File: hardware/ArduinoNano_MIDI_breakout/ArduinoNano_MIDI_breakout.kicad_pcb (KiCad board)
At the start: 2 copper layers, 68.7 x 101.3 mm, 39 parts, among them J2 MIDI OUT, J3 MIDI IN, J4 I2C, J5 Conn_01x15_Male, J6 Conn_01x15_Male, J7 Barrel_Jack_Switch, Q1 2N3904, SW1 RotaryEncoder_Switch, SW2 SW_Push, SW3 SW_Push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

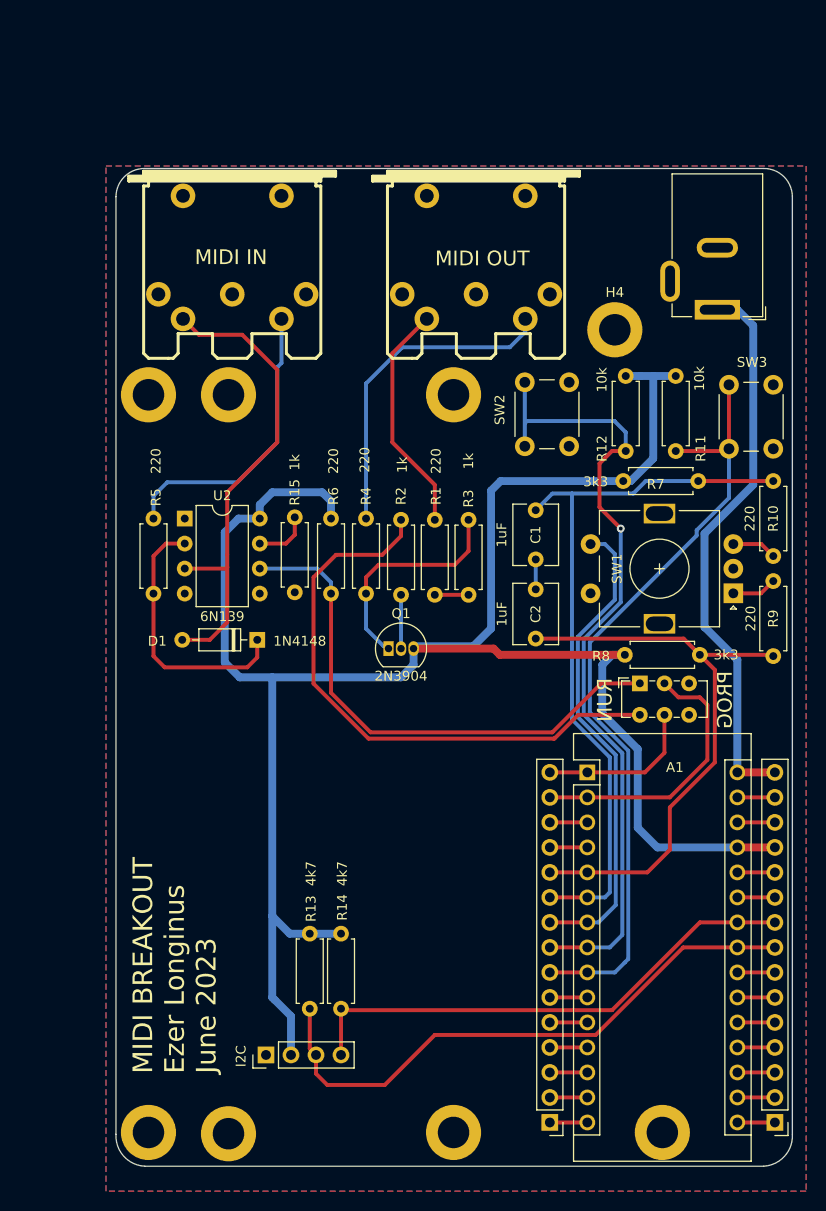
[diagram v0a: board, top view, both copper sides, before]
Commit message: Fixed MIDI pinout swap
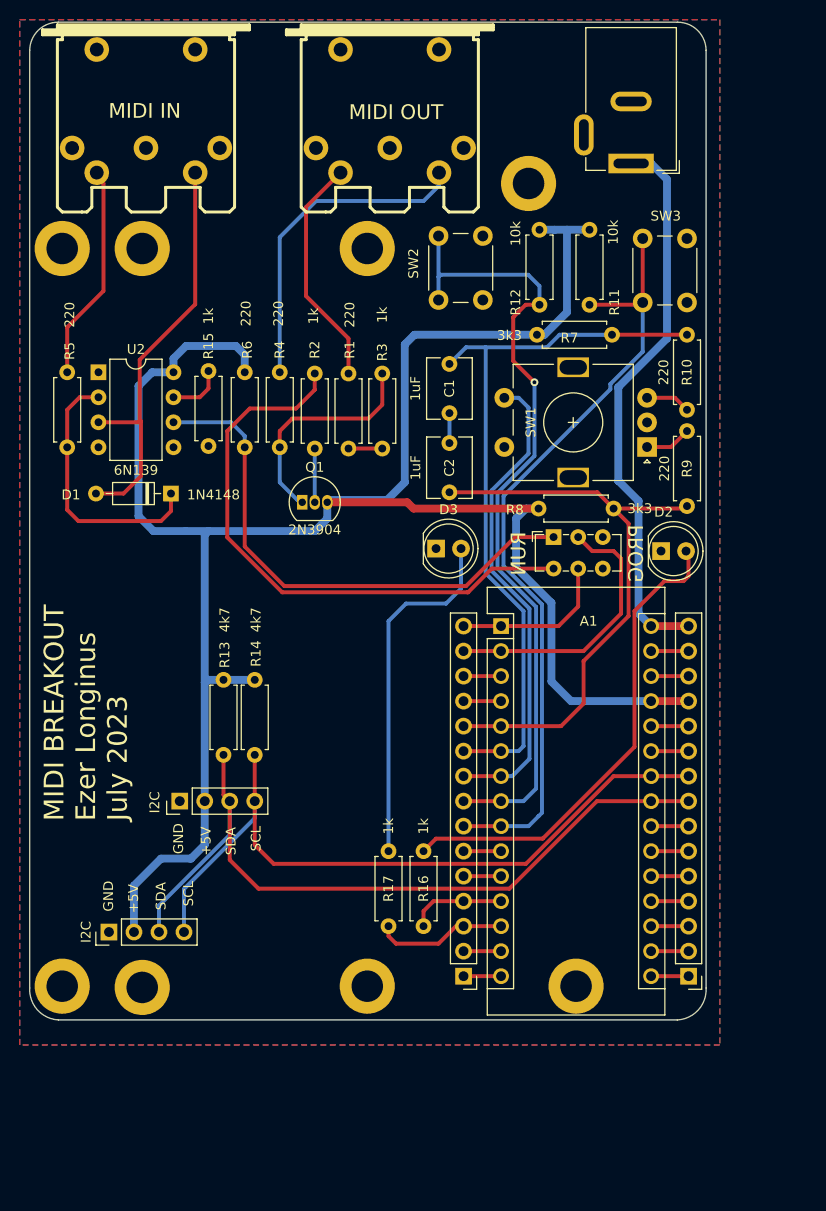
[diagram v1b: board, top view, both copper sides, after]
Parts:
- added D2: LED, LED_THT:LED_D5.0mm, F.Cu at (168.8, 94.4)
- added D3: LED, LED_THT:LED_D5.0mm, F.Cu at (145.9, 94.1)
- added I2C: I2C, Connector_PinHeader_2.54mm:PinHeader_1x04_P2.54mm_Vertical, F.Cu at (112.7, 133.1)
- added R16: 1k, Resistor_THT:R_Axial_DIN0207_L6.3mm_D2.5mm_P7.62mm_Horizontal, F.Cu at (144.7, 132.5)
- added R17: 1k, Resistor_THT:R_Axial_DIN0207_L6.3mm_D2.5mm_P7.62mm_Horizontal, F.Cu at (141.1, 132.5)
- moved J4 27.2 mm to (119.9, 119.8)
- moved R13 27.2 mm to (124.3, 115.1)
- moved R14 27.2 mm to (127.5, 115.1)
- moved R9 17.6 mm to (171.4, 89.8)
- moved A1 17.3 mm to (152.5, 102.0)
- moved C2 17.3 mm to (147.3, 88.4)
- moved H1 17.3 mm to (160.1, 138.6)
- moved H6 17.3 mm to (138.9, 138.6)
- moved J2 17.3 mm to (141.2, 50.4)
- moved J5 17.3 mm to (171.6, 137.5)
- moved R1 17.3 mm to (137.0, 76.3)
- moved R15 17.3 mm to (122.8, 76.1)
- moved R3 17.3 mm to (140.5, 76.3)
- moved R4 17.3 mm to (130.0, 83.8)
- moved SW4 17.3 mm to (157.9, 92.9)
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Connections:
- J3 pad 4: Net-(D1-Pad2) -> Net-(J3-Pad4)
- J3 pad 5: Net-(J3-Pad5) -> Net-(D1-Pad2)
- R5 pad 1: Net-(J3-Pad5) -> Net-(J3-Pad4)
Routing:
- net Net-(D2-Pad2): track 0.00 -> 49.1 mm
- net Net-(D3-Pad2): track 0.00 -> 36.2 mm
- net Net-(J3-Pad5): track 30.1 -> 0.00 mm
- net Net-(J3-Pad4): track 0.00 -> 22.1 mm
- net SCL1: track 52.5 -> 74.0 mm
- net SDA1: track 60.4 -> 79.4 mm
- net D10: track 3.81 -> 13.5 mm
- net D9: track 3.81 -> 9.82 mm
- net Net-(D1-Pad2): track 49.1 -> 43.3 mm
- net +5V: track 208.9 -> 212.8 mm
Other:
- board text added: "+5V"
- board text added: "GND"
- board text added: "MIDI BREAKOUT Ezer Longinus July 2023"
- board text added: "SCL"
- board text added: "SDA"
- board text removed: "MIDI BREAKOUT Ezer Longinus June 2023"

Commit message: Fixes to Nano Breakout
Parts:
- added kibuzzard-64B16D4A: G***, kibuzzard-64B16D4A, F.Cu at (111.6, 109.1)
- SW4: footprint Button_Switch_THT:SW_E-Switch_EG1271_DPDT -> Button_Switch_THT:SW_CuK_JS202011CQN_DPDT_Straight
- moved A1 0.18 mm to (152.7, 102.0)
- renumbered I2C to J1
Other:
- board text removed: "MIDI BREAKOUT Ezer Longinus July 2023"
